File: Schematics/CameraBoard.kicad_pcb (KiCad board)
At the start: 2 copper layers, 53 parts, among them IC1 LM3940IS-3.3_NOPB, J1 Runcam Split 4 v2, J2 USB_C_Receptacle, J4 Runcam Split 4 v2, J5 Runcam Split 4 v2, SW1 SW_Push, SW2 SW_Push, U1 STM32F405RGTx, U2 TPS22917DBVR, U3 TPS22917DBVR, U4 SN65HVD230DR, U6 TPS22917DBVR

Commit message: first PCB Draft
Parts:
- added C17: 1u, Capacitor_SMD:C_0805_2012Metric_Pad1.18x1.45mm_HandSolder, F.Cu at (82.7, 79.5)
- added C18: 100nf, Capacitor_SMD:C_0805_2012Metric_Pad1.18x1.45mm_HandSolder, F.Cu at (102.0, 71.0)
- C10: value 10u -> 100nf
- C3: value .47u -> 1u
- moved R4 81.6 mm to (61.4, 98.7)
- moved R3 80.8 mm to (61.9, 84.2)
- moved J2 74.7 mm to (91.9, 105.7)
- moved J_BUCK_IN_A1 73.0 mm to (54.0, 41.5)
- moved J_BUCK_IN_B1 73.0 mm to (54.0, 44.5)
- moved D1 72.2 mm to (95.2, 97.4)
- moved J_BUCK_OUT_A1 72.0 mm to (54.0, 48.5), turned to 180 degrees
- moved IC1 71.8 mm to (78.5, 46.0)
- moved U6 71.3 mm to (178.9, 63.5)
- moved J_BUCK_OUT_B1 71.0 mm to (54.0, 52.5), turned to 180 degrees
- moved C11 69.2 mm to (72.0, 58.0), turned to -90 degrees
- moved C7 67.9 mm to (164.8, 64.5), turned to 180 degrees
- moved C3 66.9 mm to (63.5, 51.0)
- moved C16 66.8 mm to (61.7, 68.1)
- moved U4 63.8 mm to (112.2, 50.7)
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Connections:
- C10 pad 2: +3.3VA -> +3.3V
- C9 pad 2: +3.3VA -> +3.3V
- FB1 pad 2: +3.3VA -> +3.3V
- J_BUCK_OUT_B1 pad 2: unconnected-(J_BUCK_OUT_B1-Pin_2-Pad2) -> GND
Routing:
- net +3.3V: track 0.00 -> 138.6 mm
- net +5V: track 0.00 -> 33.3 mm
- net /usb_type_c/D+: track 0.00 -> 12.7 mm, vias 0 -> 3
- net /usb_type_c/D-: track 0.00 -> 10.6 mm
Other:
- board outline added: 103.5 x 71.5 mm

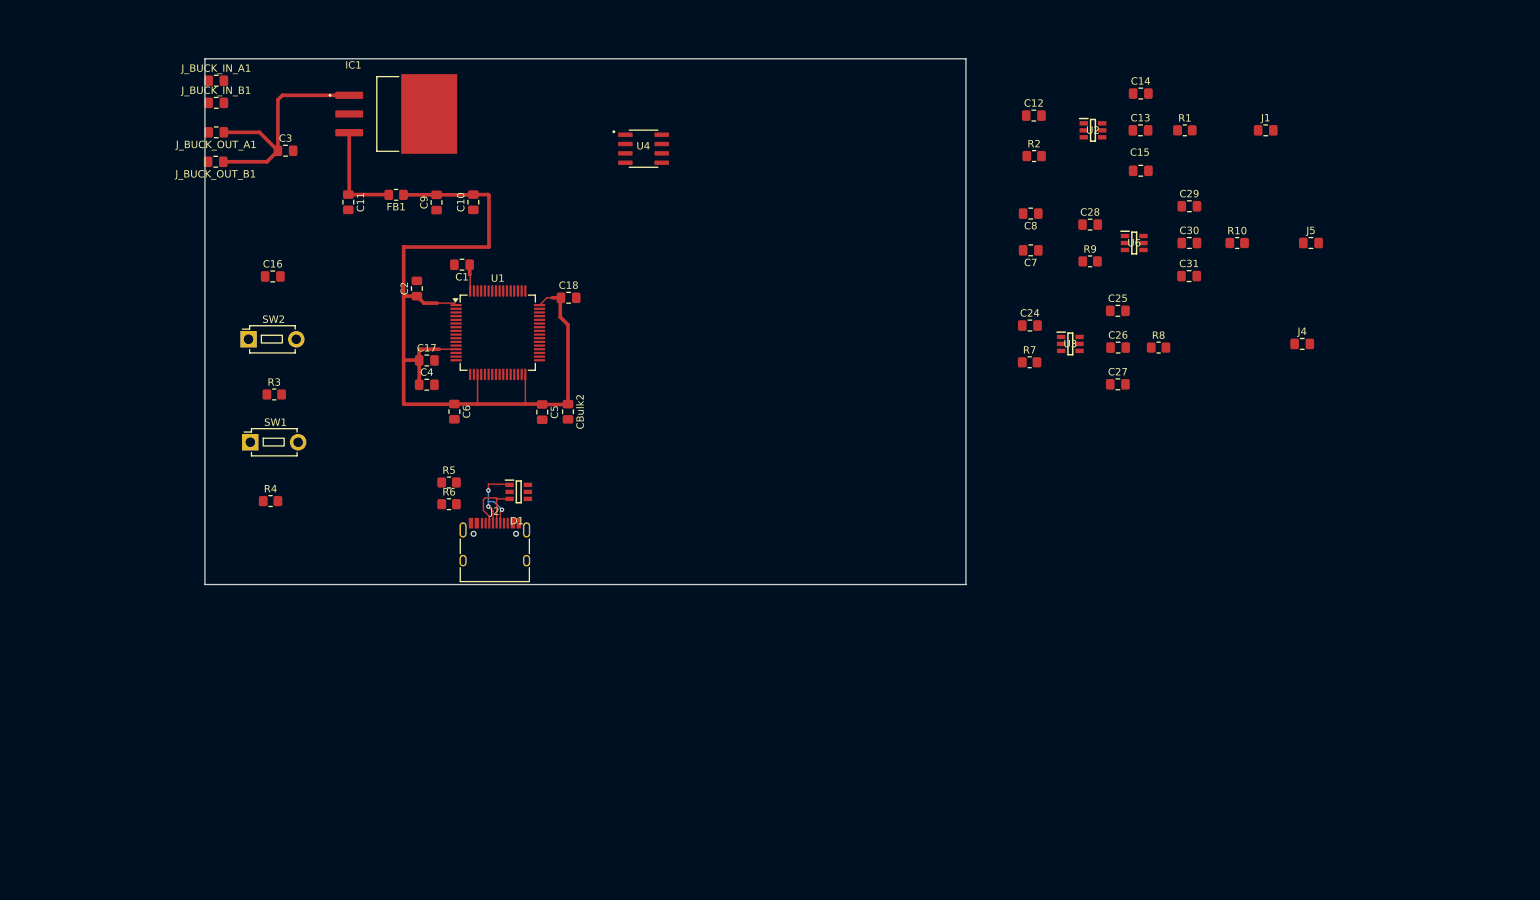
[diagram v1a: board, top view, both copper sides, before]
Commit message: fixing duplicate project files and fixing github merge conflict
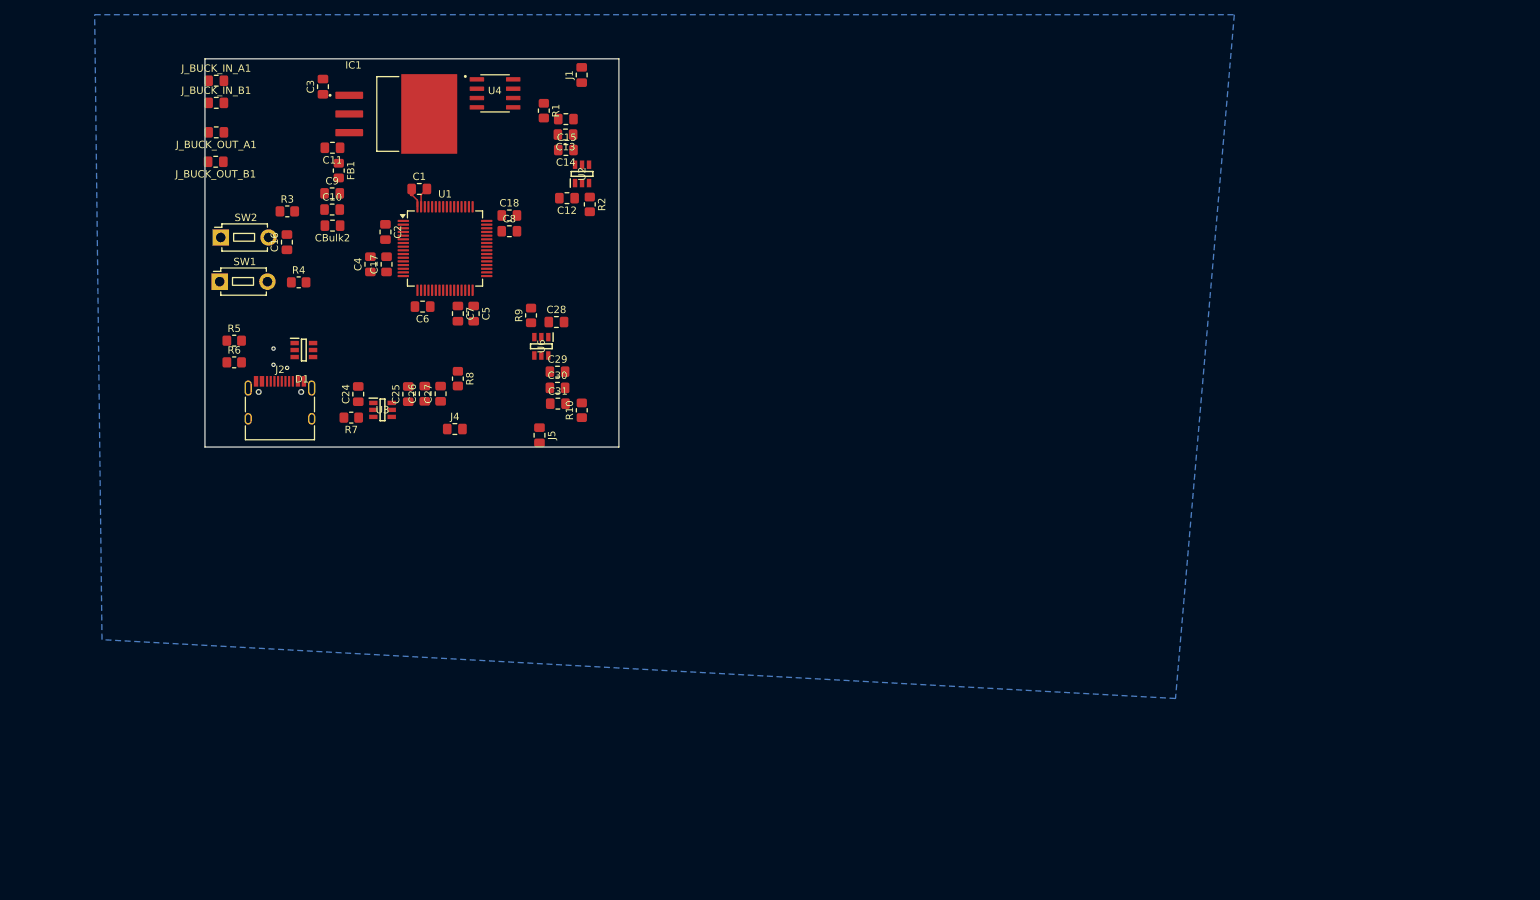
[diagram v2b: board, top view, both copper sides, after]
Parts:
- moved J4 115.8 mm to (86.5, 88.8)
- moved J5 108.1 mm to (98.0, 89.7), turned to -90 degrees
- moved C25 97.2 mm to (80.2, 84.1), turned to 90 degrees
- moved R8 95.4 mm to (86.9, 82.0), turned to -90 degrees
- moved C26 94.5 mm to (82.4, 84.0), turned to 90 degrees
- moved U3 94.0 mm to (76.7, 86.2)
- moved J1 93.3 mm to (103.7, 40.7), turned to 90 degrees
- moved R7 92.6 mm to (72.4, 87.3), turned to 180 degrees
- moved C27 92.1 mm to (84.5, 84.0), turned to 90 degrees
- moved R10 92.0 mm to (103.8, 86.3), turned to 90 degrees
- moved C24 91.8 mm to (73.3, 84.1), turned to 90 degrees
- moved C29 88.8 mm to (100.5, 81.0)
- moved C30 88.2 mm to (100.5, 83.2)
- moved C31 87.6 mm to (100.5, 85.4)
- moved R1 87.2 mm to (98.6, 45.5), turned to -90 degrees
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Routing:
- net +3.3V: track 138.6 -> 3.23 mm
- net +5V: track 33.3 -> 0.00 mm
- net /usb_type_c/D+: track 12.7 -> 0.00 mm
- net /usb_type_c/D-: track 10.6 -> 0.00 mm
- net GND: track 0.00 -> 2.75 mm
- added copper zone on B.Cu, net GND
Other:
- board size 103.5 x 71.5 mm -> 56.3 x 52.8 mm

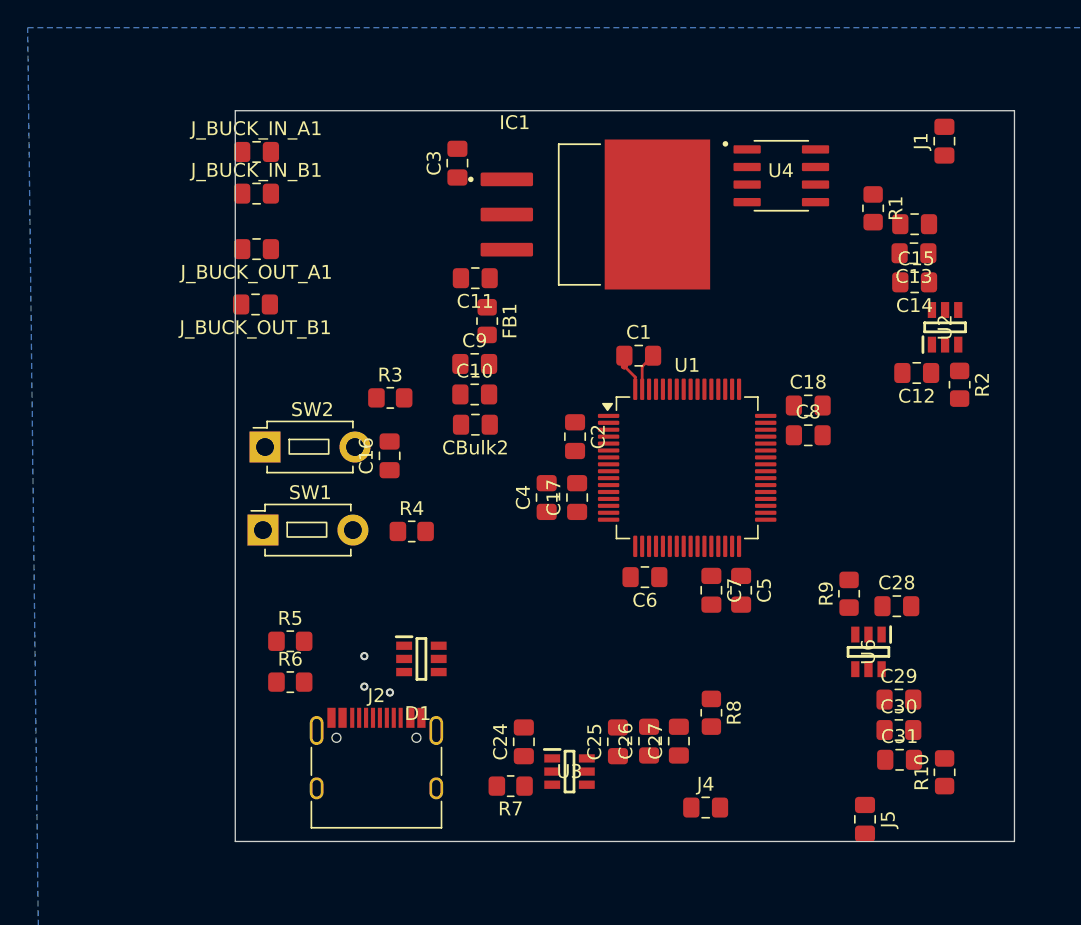
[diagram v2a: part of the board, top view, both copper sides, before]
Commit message: Replaced LDO with smaller & Fixed resistor value for Camera tx lines
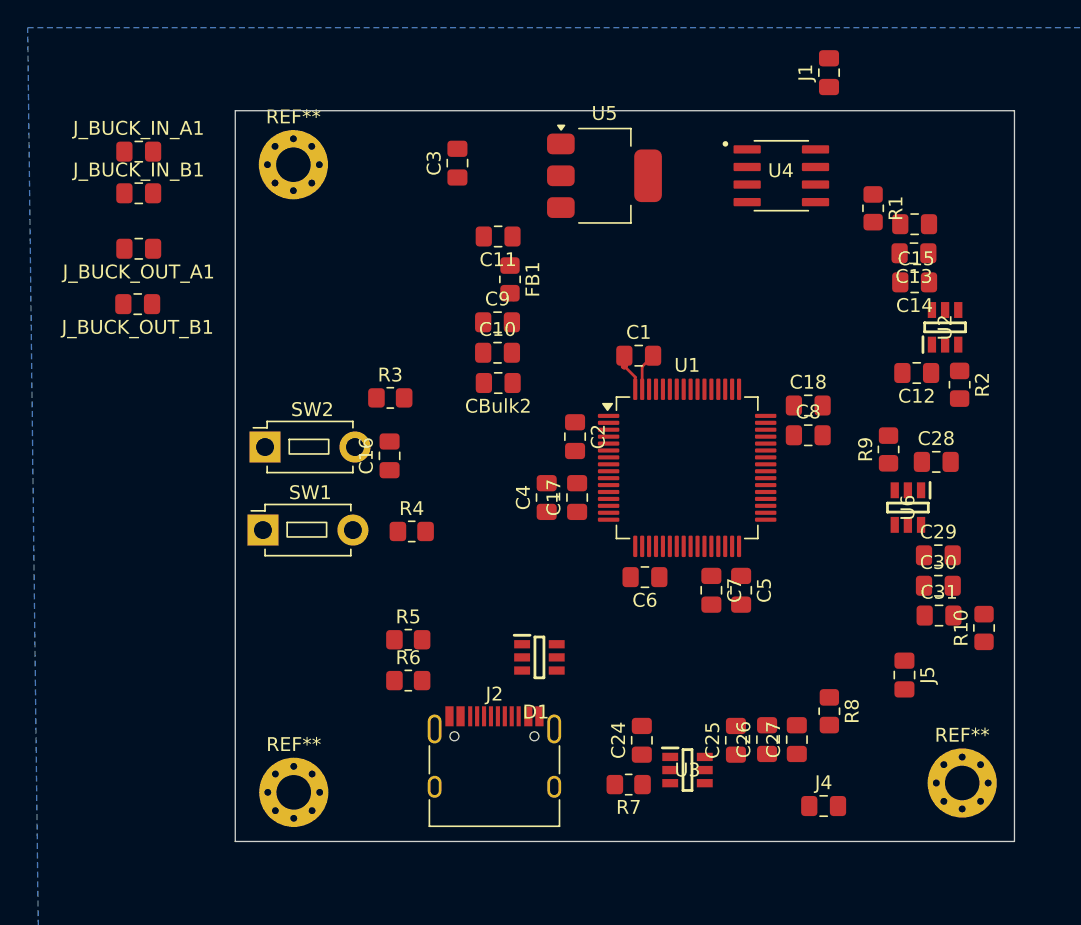
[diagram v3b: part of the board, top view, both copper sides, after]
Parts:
- removed IC1: LM3940IS-3.3_NOPB, myFootprints:TO254P1524X483-4N
- added REF**: MountingHole_2.5mm_Pad_Via, MountingHole:MountingHole_2.5mm_Pad_Via, F.Cu at (105.0, 87.1)
- added REF**: MountingHole_2.5mm_Pad_Via, MountingHole:MountingHole_2.5mm_Pad_Via, F.Cu at (56.7, 87.8)
- added REF**: MountingHole_2.5mm_Pad_Via, MountingHole:MountingHole_2.5mm_Pad_Via, F.Cu at (56.7, 42.4)
- added U5: AMS1117-3.3, Package_TO_SOT_SMD:SOT-223-3_TabPin2, F.Cu at (79.2, 43.2)
- R1: value 22k -> 1k
- moved C31 10.8 mm to (103.3, 75.0)
- moved R9 10.8 mm to (99.7, 63.0)
- moved C28 10.8 mm to (103.2, 63.9)
- moved C29 10.8 mm to (103.3, 70.6)
- moved C30 10.8 mm to (103.3, 72.8)
- moved J5 10.8 mm to (100.8, 79.3)
- moved R10 10.8 mm to (106.6, 75.9)
- moved U6 10.8 mm to (101.1, 67.2)
- moved J1 9.70 mm to (95.4, 35.8)
- moved C24 8.53 mm to (81.9, 84.0)
- moved C27 8.53 mm to (93.1, 83.9)
- moved J4 8.53 mm to (95.0, 88.7)
- moved R5 8.53 mm to (65.0, 76.7)
- moved R6 8.53 mm to (65.0, 79.7)
- moved C25 8.53 mm to (88.7, 84.0)
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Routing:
- net /usb_type_c/D+: vias 3 -> 0

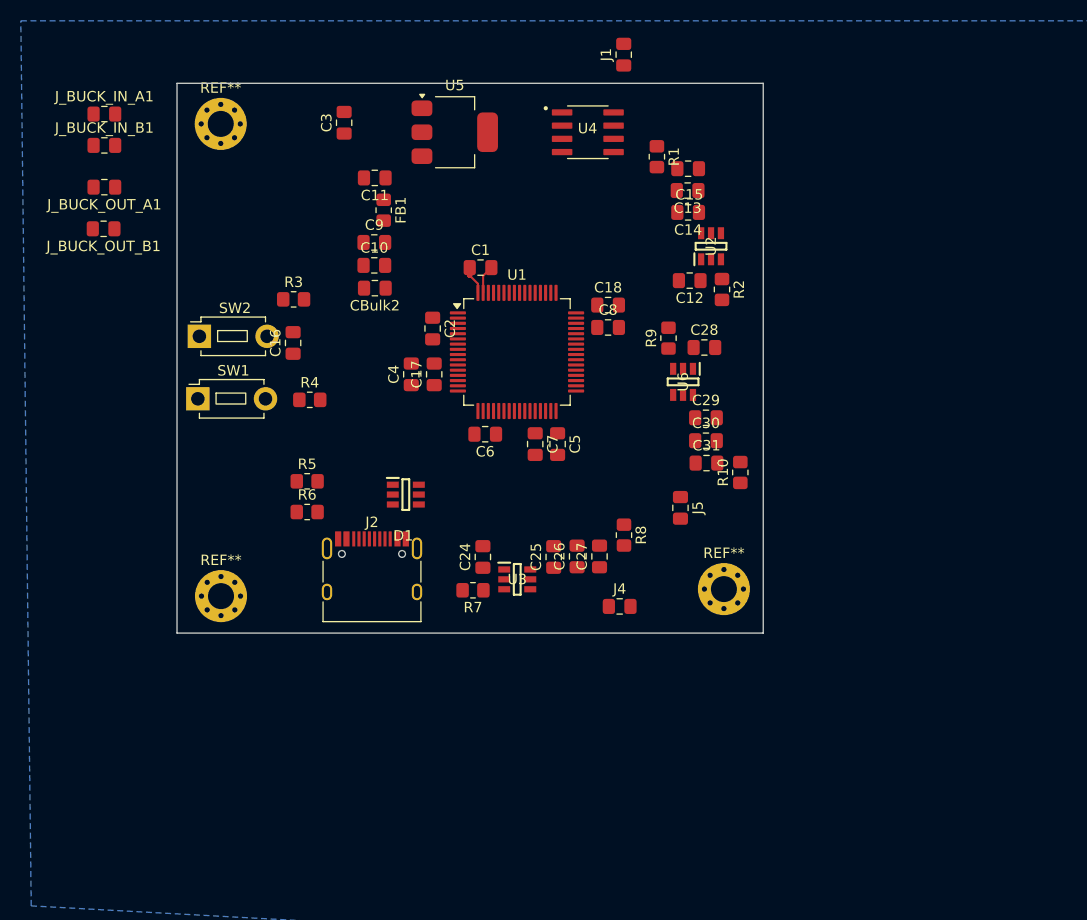
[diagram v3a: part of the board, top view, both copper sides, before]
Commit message: added pin headers for connectors and added buck connector connections, rounding done and mounting holes included, routing will occur after review
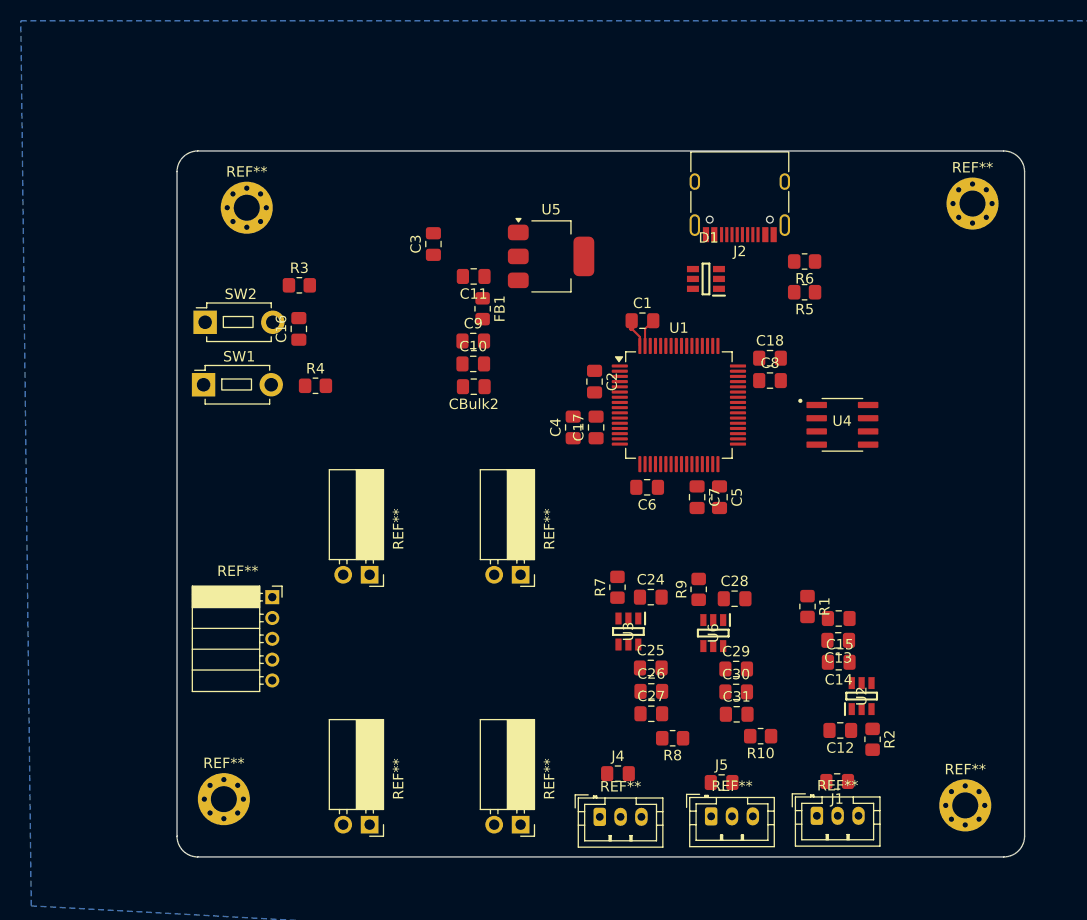
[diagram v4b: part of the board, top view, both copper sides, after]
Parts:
- removed J_BUCK_IN_A1, J_BUCK_IN_B1, J_BUCK_OUT_A1, J_BUCK_OUT_B1: ~, Capacitor_SMD:C_0805_2012Metric_Pad1.18x1.45mm_HandSolder
- added REF**: JST_PH_B3B-PH-K_1x03_P2.00mm_Vertical, Connector_JST:JST_PH_B3B-PH-K_1x03_P2.00mm_Vertical, F.Cu at (103.8, 108.9)
- added REF**: PinSocket_1x02_P2.54mm_Horizontal, Connector_PinSocket_2.54mm:PinSocket_1x02_P2.54mm_Horizontal, F.Cu at (85.5, 85.7)
- added REF**: JST_PH_B3B-PH-K_1x03_P2.00mm_Vertical, Connector_JST:JST_PH_B3B-PH-K_1x03_P2.00mm_Vertical, F.Cu at (93.1, 109.0)
- added REF**: PinSocket_1x02_P2.54mm_Horizontal, Connector_PinSocket_2.54mm:PinSocket_1x02_P2.54mm_Horizontal, F.Cu at (85.5, 109.7)
- added REF**: JST_PH_B3B-PH-K_1x03_P2.00mm_Vertical, Connector_JST:JST_PH_B3B-PH-K_1x03_P2.00mm_Vertical, F.Cu at (114.0, 108.8)
- added REF**: PinSocket_1x02_P2.54mm_Horizontal, Connector_PinSocket_2.54mm:PinSocket_1x02_P2.54mm_Horizontal, F.Cu at (71.0, 85.7)
- added REF**: PinSocket_1x02_P2.54mm_Horizontal, Connector_PinSocket_2.54mm:PinSocket_1x02_P2.54mm_Horizontal, F.Cu at (71.0, 109.7)
- added REF**: PinSocket_1x05_P2.00mm_Horizontal, Connector_PinSocket_2.00mm:PinSocket_1x05_P2.00mm_Horizontal, F.Cu at (61.6, 87.8)
- added REF**: MountingHole_2.5mm_Pad_Via, MountingHole:MountingHole_2.5mm_Pad_Via, F.Cu at (128.9, 50.0)
- moved J1 72.7 mm to (115.9, 105.5), turned to 180 degrees
- moved R6 53.5 mm to (112.8, 55.6), turned to 180 degrees
- moved J2 51.4 mm to (106.5, 49.0), turned to 180 degrees
- moved R5 51.1 mm to (112.8, 58.6), turned to 180 degrees
- moved C12 45.6 mm to (116.2, 100.7)
- moved C13 45.6 mm to (116.0, 92.0)
- moved C14 45.6 mm to (116.0, 94.1)
- moved C15 45.6 mm to (116.0, 89.9)
- moved R1 45.6 mm to (113.0, 88.8)
- moved R2 45.6 mm to (119.3, 101.5)
- moved U2 45.6 mm to (118.2, 97.3)
- moved U4 37.2 mm to (116.4, 71.3)
- moved D1 35.5 mm to (103.3, 57.3), turned to 180 degrees
- moved REF** 31.1 mm to (128.2, 107.8)
- moved J5 26.7 mm to (104.8, 105.7), turned to 0 degrees
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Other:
- board size 56.3 x 52.8 mm -> 81.4 x 67.8 mm

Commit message: fixed spacing issues
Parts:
- removed J4, J5: Runcam Split 4 v2, Capacitor_SMD:C_0805_2012Metric_Pad1.18x1.45mm_HandSolder
- moved SW1 51.0 mm to (105.7, 61.5), turned to 180 degrees
- moved SW2 48.7 mm to (103.7, 56.8), turned to 90 degrees
- moved C16 42.6 mm to (104.3, 47.8), turned to 180 degrees
- moved R3 37.3 mm to (100.1, 47.8), turned to 90 degrees
- moved C3 32.5 mm to (76.9, 86.5), turned to 180 degrees
- moved REF** 32.4 mm to (61.4, 55.5)
- moved U4 32.2 mm to (92.5, 49.7), turned to 90 degrees
- moved R4 29.8 mm to (95.0, 61.4), turned to 180 degrees
- moved R5 25.2 mm to (87.6, 59.2)
- moved R6 25.2 mm to (87.6, 56.2)
- moved D1 25.2 mm to (78.2, 57.9)
- moved J2 25.2 mm to (81.4, 49.6)
- moved U5 21.5 mm to (80.0, 75.0), turned to 90 degrees
- moved C25 18.3 mm to (80.2, 99.1)
- moved C26 18.3 mm to (80.3, 101.3)
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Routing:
- net +3.3V: track 3.23 -> 0.22 mm
- net GND: track 2.75 -> 0.00 mm
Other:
- board size 81.4 x 67.8 mm -> 62.3 x 68 mm
